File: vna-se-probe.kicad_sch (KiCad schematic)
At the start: 4 parts, among them J2 Harwin_1x1_H2.4mm_Pad1.7mm_P7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, J3 Harwin_1x1_H2.4mm_Pad1.7mm_P7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, J4 Conn_SMA_RF2-143-T-17-50-G

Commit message: [#75263] Update project
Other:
- company: (none) -> Antmicro Ltd
- title: (none) -> VNA SE probe
- moved on the sheet: H1, J2, J3, J4

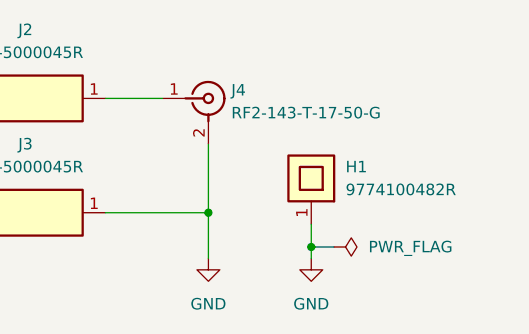
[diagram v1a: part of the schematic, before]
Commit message: [#75263] Adjust via, clean DRC and ERC
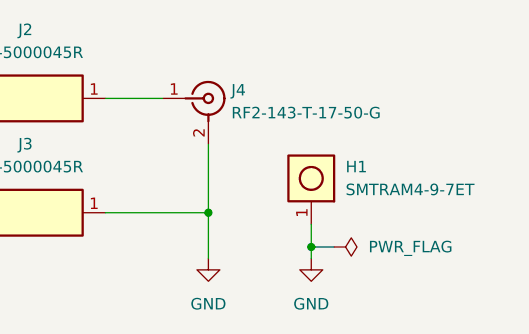
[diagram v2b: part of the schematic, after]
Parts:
- removed H1: SMTRAM4-9-7ET, antmicro-footprints:SMTRAM4-9-7ET, symbol antmicroMechanicalParts:SMTRAM4-9-7ET
- added H1: MP_Terminal_M4_SMD_Horizontal_SMTRAM4-9-7ET, antmicro-footprints:MP_Terminal_M4_SMD_Horizontal_SMTRAM4-9-7ET, symbol antmicroMechanicalParts:MP_Terminal_M4_SMD_Horizontal_SMTRAM4-9-7ET
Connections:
- net GND: now also H1.1
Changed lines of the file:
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@@
 			)
 		)
-		(property "Datasheet" "https://www.tme.eu/Document/613028b507cfc72671e78c1d2ad14b1d/RF2-154-T-17-50-G.pdf"
+		(property "Datasheet" "https://www.tme.eu/Document/5895dbb620da9c3499391e7670c4adea/RF2-143-T-17-50-G.pdf"
 			(at 222.25 134.62 0)
 			(effects
@@
 				(path "/397d0a83-0126-436a-9cf1-8bcf1fa47f98"
 					(reference "#FLG01")
-					(unit 1)
-				)
-			)
-		)
-	)
-	(symbol
-		(lib_id "antmicroMechanicalParts:SMTRAM4-9-7ET")
-		(at 218.44 140.97 90)
-		(unit 1)
-		(exclude_from_sim no)
-		(in_bom yes)
-		(on_board yes)
-		(dnp no)
-		(fields_autoplaced yes)
-		(property "Reference" "H1"
-			(at 222.25 134.62 90)
-			(effects
-				(font
-					(size 1.27 1.27)
-					(thickness 0.15)
-				)
-				(justify right)
-			)
-		)
-		(property "Value" "SMTRAM4-9-7ET"
-			(at 226.06 118.11 0)
-			(effects
-				(font
-					(size 1.27 1.27)
-					(thickness 0.15)
-				)
-				(justify left bottom)
-				(hide yes)
-			)
-		)
-		(property "Footprint" "antmicro-footprints:SMTRAM4-9-7ET"
-			(at 228.6 118.11 0)
-			(effects
-				(font
-					(size 1.27 1.27)
-					(thickness 0.15)
-				)
-				(justify left bottom)
-				(hide yes)
-			)
-		)
-		(property "Datasheet" "https://www.pemnet.com/eu/wp-content/uploads/sites/9/2022/06/radata.pdf"
-			(at 231.14 118.11 0)
-			(effects
-				(font
-					(size 1.27 1.27)
-					(thickness 0.15)
-				)
-				(justify left bottom)
-				(hide yes)
-			)
-		)
-		(property "Description" "Spacer, SMT, Steel, M4 Thread"
-			(at 218.44 140.97 0)
-			(effects
-				(font
-					(size 1.27 1.27)
-				)
-				(hide yes)
-			)
-		)
-		(property "Manufacturer" "Würth Elektronik"
-			(at 233.68 118.11 0)
-			(effects
-				(font
-					(size 1.27 1.27)
-					(thickness 0.15)
-				)
-				(justify left bottom)
-				(hide yes)
-			)
-		)
-		(property "MPN" "9774100482R"
-			(at 222.25 137.16 90)
-			(effects
-				(font
-					(size 1.27 1.27)
-					(thickness 0.15)
-				)
-				(justify right)
-			)
-		)
-		(property "Author" "Antmicro"
-			(at 236.22 118.11 0)
-			(effects
-				(font
-					(size 1.27 1.27)
-					(thickness 0.15)
-				)
-				(justify left bottom)
-				(hide yes)
-			)
-		)
-		(property "License" "Apache-2.0"
-			(at 238.76 118.11 0)
-			(effects
-				(font
-					(size 1.27 1.27)
-					(thickness 0.15)
-				)
-				(justify left bottom)
-				(hide yes)
-			)
-		)
-		(pin "1"
-		)
-		(instances
-			(project ""
-				(path "/397d0a83-0126-436a-9cf1-8bcf1fa47f98"
-					(reference "H1")
 					(unit 1)
 				)
@@
 					(unit 1)
 				)
+			)
+		)
+	)
+	(symbol
+		(lib_id "antmicroMechanicalParts:MP_Terminal_M4_SMD_Horizontal_SMTRAM4-9-7ET")
+		(at 218.44 140.97 90)
+		(unit 1)
+		(exclude_from_sim no)
+		(in_bom no)
+		(on_board yes)
+		(dnp no)
+		(fields_autoplaced yes)
+		(property "Reference" "H1"
+			(at 222.25 134.62 90)
+			(effects
+				(font
+					(size 1.27 1.27)
+					(thickness 0.15)
+				)
+				(justify right)
+			)
+		)
+		(property "Value" "MP_Terminal_M4_SMD_Horizontal_SMTRAM4-9-7ET"
+			(at 223.266 118.11 0)
+			(effects
+				(font
+					(size 1.27 1.27)
+					(thickness 0.15)
+				)
+				(justify left bottom)
+				(hide yes)
+			)
+		)
+		(property "Footprint" "antmicro-footprints:MP_Terminal_M4_SMD_Horizontal_SMTRAM4-9-7ET"
+			(at 225.298 118.11 0)
+			(effects
+				(font
+					(size 1.27 1.27)
+					(thickness 0.15)
+				)
+				(justify left bottom)
+				(hide yes)
+			)
+		)
+		(property "Datasheet" "https://www.pemnet.com/eu/wp-content/uploads/sites/9/2022/06/radata.pdf"
+			(at 227.33 118.11 0)
+			(effects
+				(font
+					(size 1.27 1.27)
+					(thickness 0.15)
+				)
+				(justify left bottom)
+				(hide yes)
+			)
+		)
+		(property "Description" "Steel spacer, SMT, M4 Thread, Horizontal"
+			(at 229.616 119.126 0)
+			(effects
+				(font
+					(size 1.27 1.27)
+				)
+				(justify left bottom)
+				(hide yes)
+			)
+		)
+		(property "Manufacturer" "PEM"
+			(at 238.76 118.11 0)
+			(effects
+				(font
+					(size 1.27 1.27)
+				)
+				(justify left bottom)
+				(hide yes)
+			)
+		)
+		(property "MPN" "SMTRAM4-9-7ET"
+			(at 222.25 137.1599 90)
+			(effects
+				(font
+					(size 1.27 1.27)
+				)
+				(justify right)
+			)
+		)
+		(property "Author" "Antmicro"
+			(at 234.188 118.11 0)
+			(effects
+				(font
+					(size 1.27 1.27)
+				)
+				(justify left bottom)
+				(hide yes)
+			)
+		)
+		(property "License" "Apache-2.0"
+			(at 231.902 118.11 0)
+			(effects
+				(font
+					(size 1.27 1.27)
+				)
+				(justify left bottom)
+				(hide yes)
+			)
+		)
+		(pin "1"
+		)
+		(instances
+			(project ""
+				(path "/397d0a83-0126-436a-9cf1-8bcf1fa47f98"
+					(reference "H1")
+					(unit 1)
+				)

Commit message: [#80183] Update pogo pin lib link
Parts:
- J2, J3: value Harwin_1x1_H2.4mm_Pad1.7mm_P70-5000045R -> Harwin_1x1_H2.4mm_Pad1.7mm_P70-5000045R_CUSTOM_EdgeMount; footprint antmicro-footprints:Harwin_1x1_H2.4mm_Pad1.7mm_P70-5000045R -> antmicro-footprints:Harwin_1x1_H2.4mm_Pad1.7mm_P70-5000045R_Edge; symbol antmicroPogoPins:Harwin_1x1_H2.4mm_Pad1.7mm_P70-5000045R -> antmicroPogoPins:Harwin_1x1_H2.4mm_Pad1.7mm_P70-5000045R_CUSTOM_EdgeMount
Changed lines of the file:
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@@
 (kicad_sch
-	(version 20231120)
+	(version 20250114)
 	(generator "eeschema")
-	(generator_version "8.0")
+	(generator_version "9.0")
 	(paper "A3")
 	(title_block
 		(title "VNA SE probe")
-		(date "2025-04-10")
-		(rev "1.0.0")
+		(date "2025-07-09")
+		(rev "1.0.1")
 		(company "Antmicro Ltd")
 		(comment 1 "www.antmicro.com")
@@
 	)
 	(symbol
-		(lib_name "Harwin_1x1_H2.4mm_Pad1.7mm_P70-5000045R_1")
-		(lib_id "antmicroPogoPins:Harwin_1x1_H2.4mm_Pad1.7mm_P70-5000045R")
+		(lib_id "antmicroPogoPins:Harwin_1x1_H2.4mm_Pad1.7mm_P70-5000045R_CUSTOM_EdgeMount")
 		(at 195.58 139.7 180)
 		(unit 1)
@@
 			)
 		)
-		(property "Value" "Harwin_1x1_H2.4mm_Pad1.7mm_P70-5000045R"
+		(property "Value" "Harwin_1x1_H2.4mm_Pad1.7mm_P70-5000045R_CUSTOM_EdgeMount"
 			(at 167.64 132.08 0)
 			(effects
@@
 			)
 		)
-		(property "Footprint" "antmicro-footprints:Harwin_1x1_H2.4mm_Pad1.7mm_P70-5000045R"
+		(property "Footprint" "antmicro-footprints:Harwin_1x1_H2.4mm_Pad1.7mm_P70-5000045R_Edge"
 			(at 167.64 129.54 0)
 			(effects
@@
 	)
 	(symbol
-		(lib_id "antmicroPogoPins:Harwin_1x1_H2.4mm_Pad1.7mm_P70-5000045R")
+		(lib_id "antmicroPogoPins:Harwin_1x1_H2.4mm_Pad1.7mm_P70-5000045R_CUSTOM_EdgeMount")
 		(at 195.58 127 180)
 		(unit 1)
@@
 			)
 		)
-		(property "Value" "Harwin_1x1_H2.4mm_Pad1.7mm_P70-5000045R"
+		(property "Value" "Harwin_1x1_H2.4mm_Pad1.7mm_P70-5000045R_CUSTOM_EdgeMount"
 			(at 167.64 119.38 0)
 			(effects
@@
 			)
 		)
-		(property "Footprint" "antmicro-footprints:Harwin_1x1_H2.4mm_Pad1.7mm_P70-5000045R"
+		(property "Footprint" "antmicro-footprints:Harwin_1x1_H2.4mm_Pad1.7mm_P70-5000045R_Edge"
 			(at 167.64 116.84 0)
 			(effects
@@
 		)
 	)
+	(embedded_fonts no)
 )

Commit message: [#80183] Update library links
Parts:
- H1: now in the parts list
- J2, J3: footprint antmicro-footprints:Harwin_1x1_H2.4mm_Pad1.7mm_P70-5000045R_Edge -> antmicro-footprints:Harwin_1x1_H2.4mm_Pad1.7mm_P70-5000045R_CUSTOM_EdgeMount
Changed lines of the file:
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@@
 			)
 		)
-		(property "Footprint" "antmicro-footprints:Harwin_1x1_H2.4mm_Pad1.7mm_P70-5000045R_Edge"
+		(property "Footprint" "antmicro-footprints:Harwin_1x1_H2.4mm_Pad1.7mm_P70-5000045R_CUSTOM_EdgeMount"
 			(at 167.64 129.54 0)
 			(effects
@@
 			)
 		)
-		(property "Footprint" "antmicro-footprints:Harwin_1x1_H2.4mm_Pad1.7mm_P70-5000045R_Edge"
+		(property "Footprint" "antmicro-footprints:Harwin_1x1_H2.4mm_Pad1.7mm_P70-5000045R_CUSTOM_EdgeMount"
 			(at 167.64 116.84 0)
 			(effects
@@
 		(unit 1)
 		(exclude_from_sim no)
-		(in_bom no)
+		(in_bom yes)
 		(on_board yes)
 		(dnp no)
